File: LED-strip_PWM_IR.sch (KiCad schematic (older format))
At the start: 15 parts, among them IC1 ATtiny85, P1 CONN_2, P2 CONN_2, Q1 8MHz, T1 IRLR2905_DPAK, U1 TSOP38238, U2 MCP1804-SOT23-5

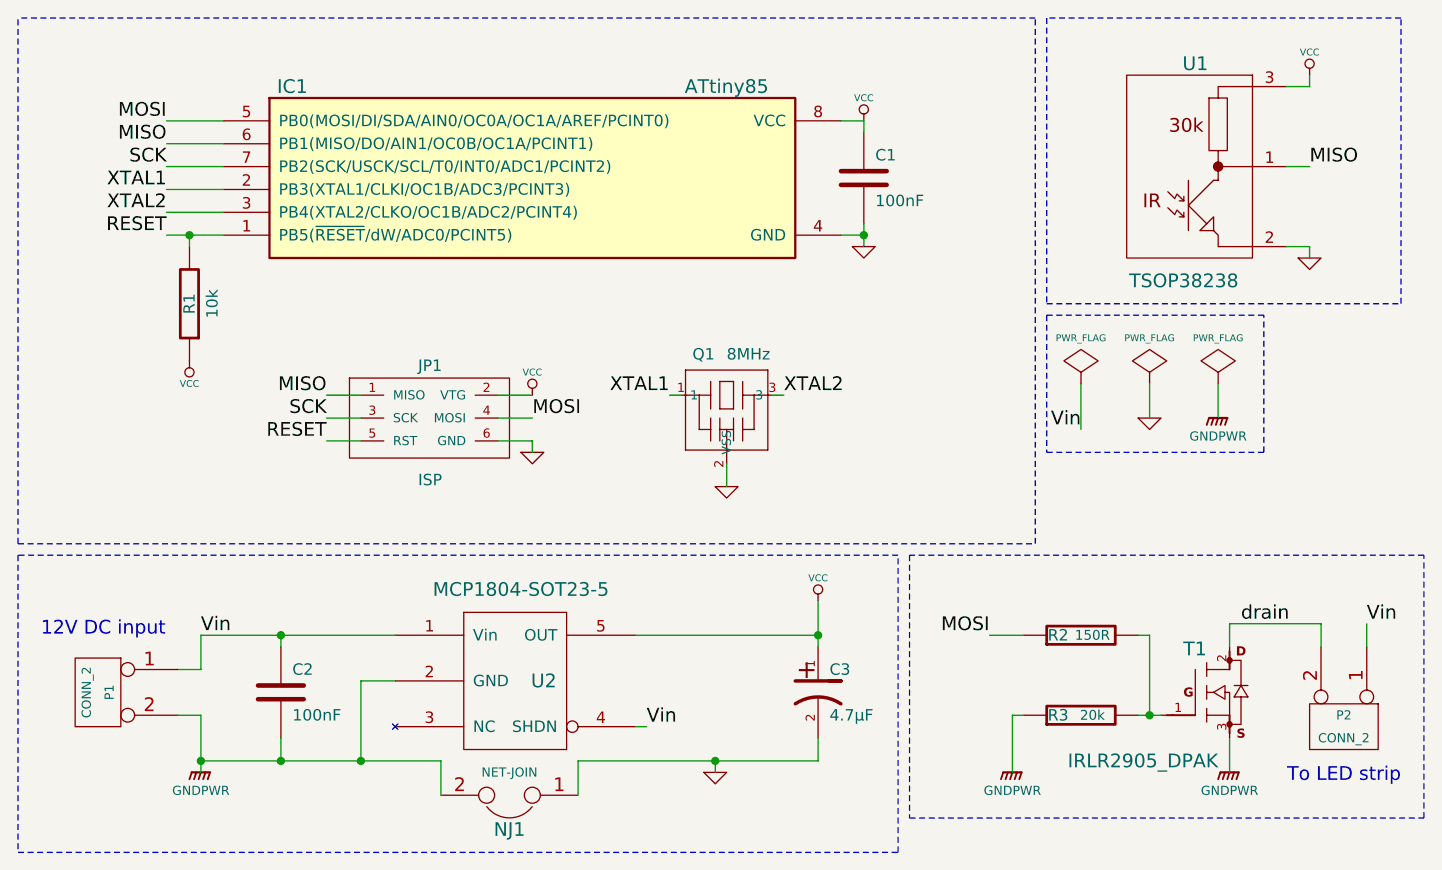
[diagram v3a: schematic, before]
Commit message: Added a LED as IR reception indicator (optional).
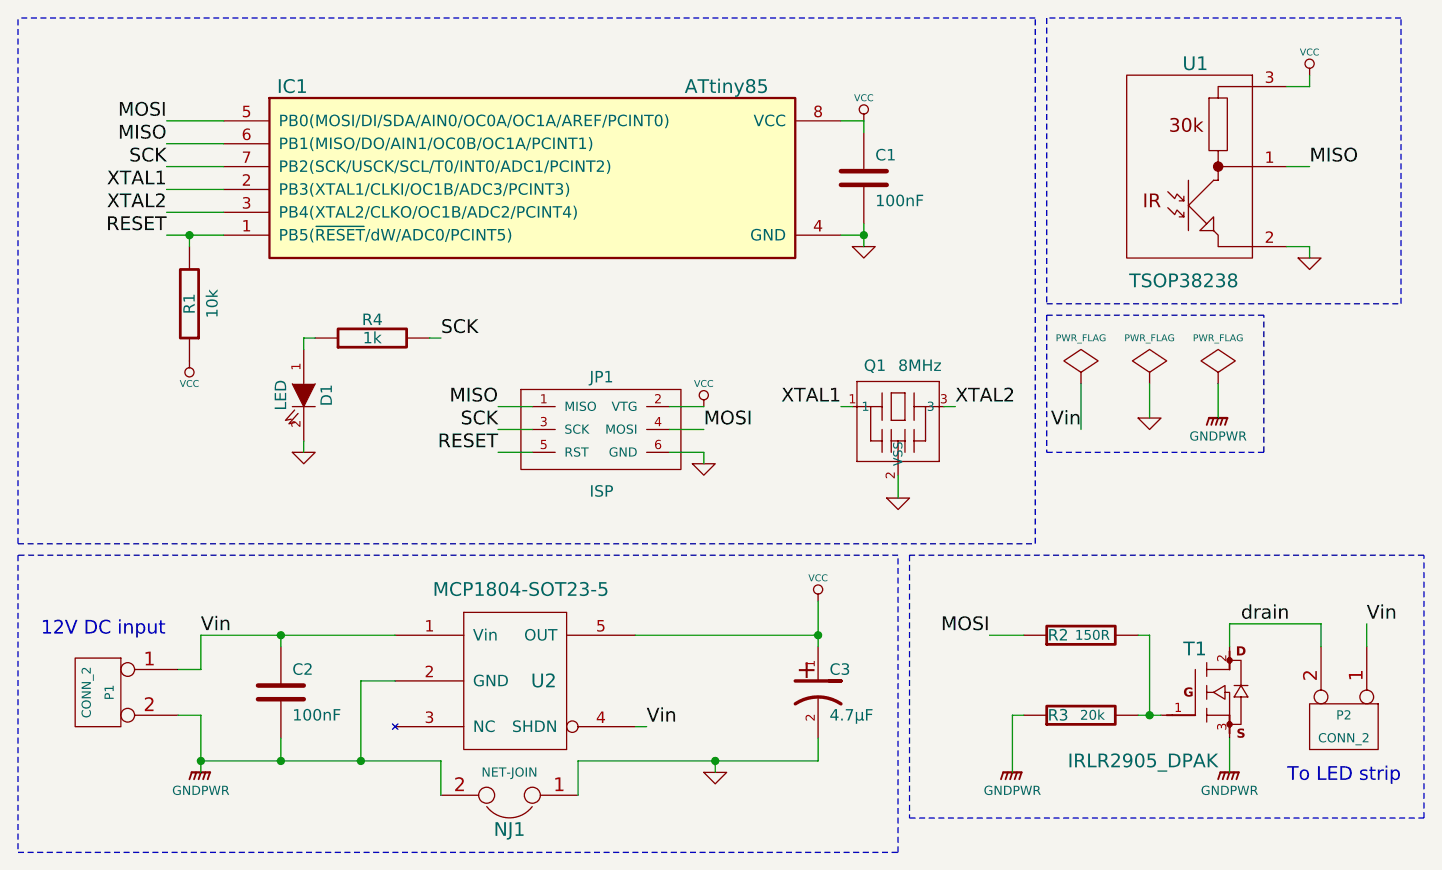
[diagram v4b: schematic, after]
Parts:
- added D1: LED, symbol LED
- added R4: 1k, symbol R
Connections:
- net GND: now also D1.2 (K)
- net SCK: now also R4.2
- new net: D1.1 (A), R4.1
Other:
- moved on the sheet: JP1, Q1
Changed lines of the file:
@@
-EESchema Schematic File Version 2  date Wed 09 Jan 2013 04:06:11 PM CET
+EESchema Schematic File Version 2  date Wed 09 Jan 2013 06:18:03 PM CET
 LIBS:my_parts
 LIBS:power
@@
 	4400 1150 4300 1150
 Wire Wire Line
-	2950 2600 2950 2550
-Wire Wire Line
-	3600 2350 3550 2350
-Wire Wire Line
-	2950 2550 2800 2550
-Wire Wire Line
-	2800 2350 2950 2350
-Wire Wire Line
-	2200 2450 2050 2450
+	3700 2650 3700 2600
+Wire Wire Line
+	4350 2400 4300 2400
+Wire Wire Line
+	3700 2600 3550 2600
+Wire Wire Line
+	3550 2400 3700 2400
+Wire Wire Line
+	2950 2500 2800 2500
 Wire Wire Line
 	1450 1650 1450 1700
 Wire Wire Line
-	2200 2350 2050 2350
-Wire Wire Line
-	2200 2550 2050 2550
-Wire Wire Line
-	2800 2450 2950 2450
-Wire Wire Line
-	3800 2650 3800 2750
-Wire Wire Line
-	4000 2350 4050 2350
+	2950 2400 2800 2400
+Wire Wire Line
+	2950 2600 2800 2600
+Wire Wire Line
+	3550 2500 3700 2500
+Wire Wire Line
+	4550 2700 4550 2800
+Wire Wire Line
+	4750 2400 4800 2400
 Wire Wire Line
 	4400 1650 4300 1650
@@
 L GND #PWR06
 U 1 1 4F6EE81E
-P 2950 2600
-F 0 "#PWR06" H 2950 2600 30  0001 C CNN
-F 1 "GND" H 2950 2530 30  0001 C CNN
-	1    2950 2600
-	1    0    0    -1
-$EndComp
-Text Label 2950 2450 0    60   ~ 0
+P 3700 2650
+F 0 "#PWR06" H 3700 2650 30  0001 C CNN
+F 1 "GND" H 3700 2580 30  0001 C CNN
+	1    3700 2650
+	1    0    0    -1
+$EndComp
+Text Label 3700 2500 0    60   ~ 0
 MOSI
 $Comp
 L VCC #PWR07
 U 1 1 4F6EE80A
-P 2950 2350
-F 0 "#PWR07" H 2950 2450 30  0001 C CNN
-F 1 "VCC" H 2950 2450 30  0000 C CNN
-	1    2950 2350
-	1    0    0    -1
-$EndComp
-Text Label 2050 2550 2    60   ~ 0
+P 3700 2400
+F 0 "#PWR07" H 3700 2500 30  0001 C CNN
+F 1 "VCC" H 3700 2500 30  0000 C CNN
+	1    3700 2400
+	1    0    0    -1
+$EndComp
+Text Label 2800 2600 2    60   ~ 0
 RESET
-Text Label 2050 2450 2    60   ~ 0
+Text Label 2800 2500 2    60   ~ 0
 SCK
-Text Label 2050 2350 2    60   ~ 0
+Text Label 2800 2400 2    60   ~ 0
 MISO
-Text Label 3550 2350 2    60   ~ 0
+Text Label 4300 2400 2    60   ~ 0
 XTAL1
-Text Label 4050 2350 0    60   ~ 0
+Text Label 4800 2400 0    60   ~ 0
 XTAL2
 $Comp
 L GND #PWR08
 U 1 1 4F6EE7AB
-P 3800 2750
-F 0 "#PWR08" H 3800 2750 30  0001 C CNN
-F 1 "GND" H 3800 2680 30  0001 C CNN
-	1    3800 2750
+P 4550 2800
+F 0 "#PWR08" H 4550 2800 30  0001 C CNN
+F 1 "GND" H 4550 2730 30  0001 C CNN
+	1    4550 2800
 	1    0    0    -1
 $EndComp
@@
 L CSTLA_T Q1
 U 1 1 4F6EC7D6
-P 3800 2350
-F 0 "Q1" H 3650 2500 50  0000 L BNN
-F 1 "8MHz" H 3800 2500 50  0000 L BNN
-F 2 "murata-resonators-CSTLA_T" H 3800 2500 50  0001 C CNN
-	1    3800 2350
+P 4550 2400
+F 0 "Q1" H 4400 2550 50  0000 L BNN
+F 1 "8MHz" H 4550 2550 50  0000 L BNN
+F 2 "murata-resonators-CSTLA_T" H 4550 2550 50  0001 C CNN
+	1    4550 2400
 	1    0    0    -1
 $EndComp
@@
 L MADW__AVR_ISP JP1
 U 1 1 4F6EC6BB
-P 2500 2450
-F 0 "JP1" H 2450 2650 50  0000 L BNN
-F 1 "ISP" H 2450 2150 50  0000 L BNN
-	1    2500 2450
+P 3250 2500
+F 0 "JP1" H 3200 2700 50  0000 L BNN
+F 1 "ISP" H 3200 2200 50  0000 L BNN
+	1    3250 2500
 	1    0    0    -1
 $EndComp
@@
 	1    0    0    -1
 $EndComp
+$Comp
+L LED D1
+U 1 1 50EDA6CA
+P 1950 2350
+F 0 "D1" H 1950 2450 50  0000 C CNN
+F 1 "LED" H 1950 2250 50  0000 C CNN
+	1    1950 2350
+	0    1    1    0
+$EndComp
+$Comp
+L GND #PWR?
+U 1 1 50EDA6D9
+P 1950 2600
+F 0 "#PWR?" H 1950 2600 30  0001 C CNN
+F 1 "GND" H 1950 2530 30  0001 C CNN
+	1    1950 2600
+	1    0    0    -1
+$EndComp
+$Comp
+L R R4
+U 1 1 50EDA6E8
+P 2250 2100
+F 0 "R4" V 2330 2100 50  0000 C CNN
+F 1 "1k" V 2250 2100 50  0000 C CNN
+	1    2250 2100
+	0    -1   -1   0
+$EndComp
+Wire Wire Line
+	1950 2550 1950 2600
+Wire Wire Line
+	1950 2150 1950 2100
+Wire Wire Line
+	1950 2100 2000 2100
+Wire Wire Line
+	2550 2100 2500 2100
+Text Label 2550 2100 0    60   ~ 0
+SCK
 $EndSCHEMATC
